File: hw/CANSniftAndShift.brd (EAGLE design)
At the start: 160 x 100 mm, 41 parts, among them CON1 FCI-10033526-N3212LF, CON4 FCI-10033526-N3212LF, IC3 TJA1050, IC4 TJA1050, IC7 FT232RL, Q1 16MHz

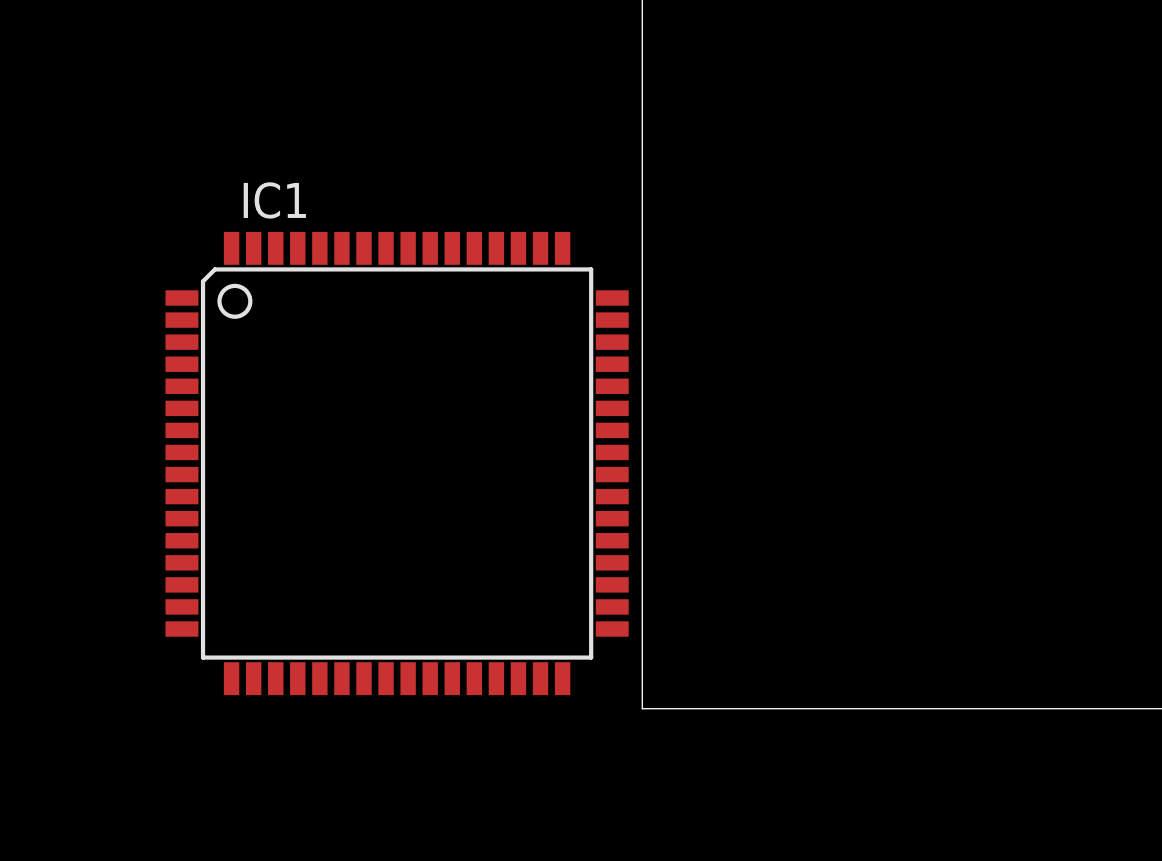
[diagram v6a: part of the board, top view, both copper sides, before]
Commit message: updated lbr AT32 package (wrong footprint used), added Dio driver, modified Port driver
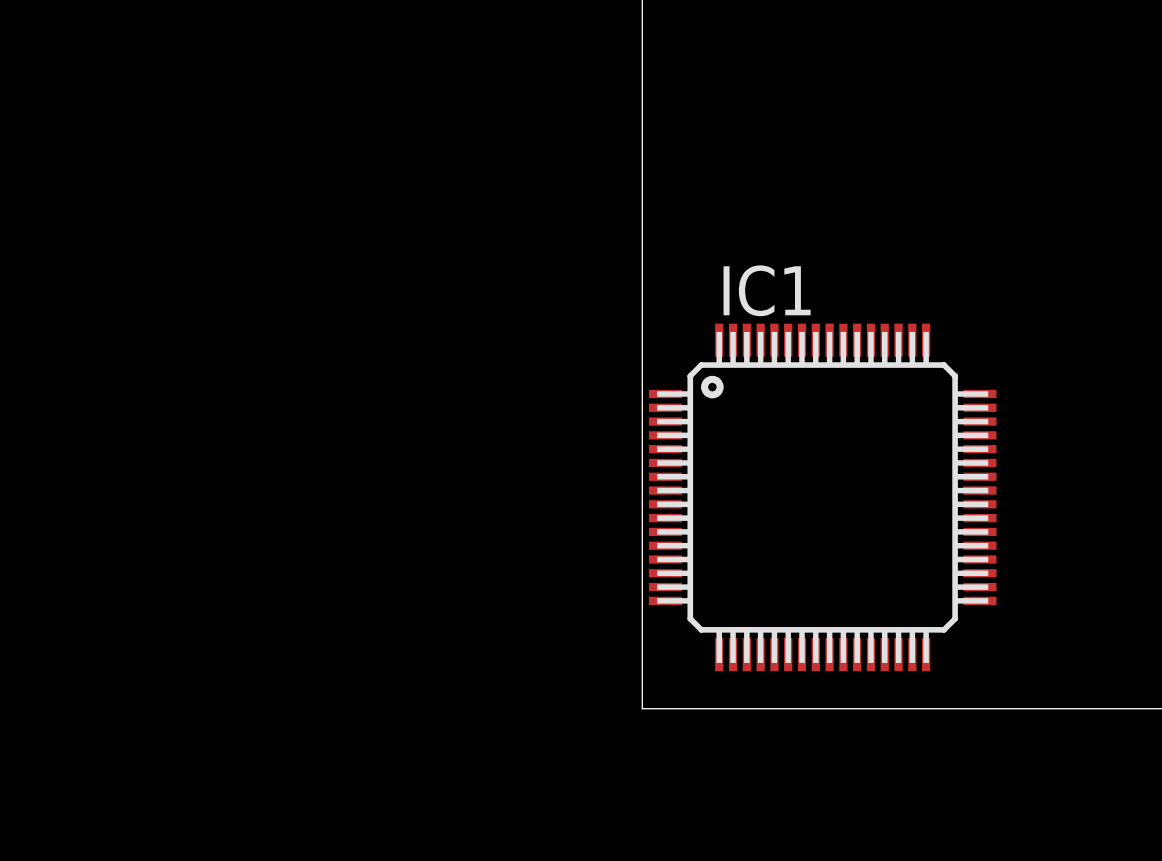
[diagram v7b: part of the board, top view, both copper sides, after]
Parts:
- IC1: device AT32UC3C264C:TQFP64 -> AT32UC3C264C:TQFP64-0.5MM
- moved IC1 15.3 mm to (6.35, 7.62)
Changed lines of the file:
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@@
 </autorouter>
 <elements>
-<element name="IC1" library="AT32UC3C264C" package="TQFP64" value="" x="-8.89" y="8.89"/>
+<element name="IC1" library="AT32UC3C264C" package="TQFP64-0.5MM" value="" x="6.35" y="7.62"/>
 <element name="Q1" library="crystal-abracon-abm3-smd" package="CRYSTAL-ABRACON-ABM7-SMD" value="16MHz" x="-13.97" y="-68.58"/>
 <element name="CON4" library="SchlegelAr_Master" package="FCI-10033526-N3212LF" value="FCI-10033526-N3212LF" x="-11.43" y="-82.55"/>
@@
 <wire x1="-76.73" y1="-306.07" x2="-45.3" y2="-250.19" width="0" layer="19" extent="1-1"/>
 <wire x1="-77.05" y1="-320.04" x2="-76.73" y2="-306.07" width="0" layer="19" extent="1-1"/>
-<wire x1="-14.89" y1="1.09" x2="-15.88" y2="-81.75" width="0" layer="19" extent="1-1"/>
-<wire x1="-7.69" y1="1.09" x2="-14.89" y2="1.09" width="0" layer="19" extent="1-1"/>
-<wire x1="-4.49" y1="1.09" x2="-7.69" y2="1.09" width="0" layer="19" extent="1-1"/>
-<wire x1="-1.09" y1="5.29" x2="-4.49" y2="1.09" width="0" layer="19" extent="1-1"/>
-<wire x1="-16.69" y1="10.89" x2="-14.89" y2="1.09" width="0" layer="19" extent="1-1"/>
-<wire x1="-5.29" y1="16.69" x2="-1.09" y2="5.29" width="0" layer="19" extent="1-1"/>
+<wire x1="2.79" y1="1.96" x2="-15.88" y2="-81.75" width="0" layer="19" extent="1-1"/>
+<wire x1="7.29" y1="1.96" x2="2.79" y2="1.96" width="0" layer="19" extent="1-1"/>
+<wire x1="9.29" y1="1.96" x2="7.29" y2="1.96" width="0" layer="19" extent="1-1"/>
+<wire x1="12.24" y1="5.41" x2="9.29" y2="1.96" width="0" layer="19" extent="1-1"/>
+<wire x1="0.84" y1="8.91" x2="2.79" y2="1.96" width="0" layer="19" extent="1-1"/>
+<wire x1="8.79" y1="13.36" x2="12.24" y2="5.41" width="0" layer="19" extent="1-1"/>
 </signal>
 <signal name="+5V">
@@
 <wire x1="-73.13" y1="-306.07" x2="-39.37" y2="-246.38" width="0" layer="19" extent="1-1"/>
 <wire x1="-76.21" y1="-314.96" x2="-73.13" y2="-306.07" width="0" layer="19" extent="1-1"/>
-<wire x1="-6.89" y1="1.09" x2="-13.03" y2="-81.75" width="0" layer="19" extent="1-1"/>
-<wire x1="-1.09" y1="4.49" x2="-6.89" y2="1.09" width="0" layer="19" extent="1-1"/>
-<wire x1="-4.49" y1="16.69" x2="-1.09" y2="4.49" width="0" layer="19" extent="1-1"/>
-<wire x1="-16.69" y1="11.69" x2="-4.49" y2="16.69" width="0" layer="19" extent="1-1"/>
+<wire x1="7.79" y1="1.96" x2="-13.03" y2="-81.75" width="0" layer="19" extent="1-1"/>
+<wire x1="12.24" y1="4.91" x2="7.79" y2="1.96" width="0" layer="19" extent="1-1"/>
+<wire x1="9.29" y1="13.36" x2="12.24" y2="4.91" width="0" layer="19" extent="1-1"/>
+<wire x1="0.84" y1="9.41" x2="9.29" y2="13.36" width="0" layer="19" extent="1-1"/>
 </signal>
 <signal name="N$2">
 <contactref element="IC1" pad="29"/>
 <contactref element="C11" pad="2"/>
-<wire x1="-5.29" y1="1.09" x2="-14.39" y2="-165.1" width="0" layer="19" extent="1-1"/>
+<wire x1="8.79" y1="1.96" x2="-14.39" y2="-165.1" width="0" layer="19" extent="1-1"/>
 </signal>
 <signal name="N$1">
 <contactref element="IC1" pad="18"/>
 <contactref element="C12" pad="2"/>
-<wire x1="-14.09" y1="1.09" x2="-14.39" y2="-170.18" width="0" layer="19" extent="1-1"/>
+<wire x1="3.29" y1="1.96" x2="-14.39" y2="-170.18" width="0" layer="19" extent="1-1"/>
 </signal>
 <signal name="N$3">
@@
 <contactref element="C13" pad="2"/>
 <wire x1="-11.82" y1="-68.58" x2="-14.39" y2="-154.94" width="0" layer="19" extent="1-1"/>
-<wire x1="-3.69" y1="1.09" x2="-11.82" y2="-68.58" width="0" layer="19" extent="1-1"/>
+<wire x1="9.79" y1="1.96" x2="-11.82" y2="-68.58" width="0" layer="19" extent="1-1"/>
 </signal>
 <signal name="N$4">
@@
 <contactref element="C14" pad="2"/>
 <wire x1="-16.12" y1="-68.58" x2="-14.39" y2="-160.02" width="0" layer="19" extent="1-1"/>
-<wire x1="-2.89" y1="1.09" x2="-16.12" y2="-68.58" width="0" layer="19" extent="1-1"/>
+<wire x1="10.29" y1="1.96" x2="-16.12" y2="-68.58" width="0" layer="19" extent="1-1"/>
 </signal>
 <signal name="USB_D-">
@@
 <contactref element="IC7" pad="1"/>
 <contactref element="IC1" pad="59"/>
-<wire x1="-10.89" y1="16.69" x2="-14.385" y2="-100.145" width="0" layer="19" extent="1-1"/>
+<wire x1="5.29" y1="13.36" x2="-14.385" y2="-100.145" width="0" layer="19" extent="1-1"/>
 </signal>
 <signal name="FTDI_RXD">
 <contactref element="IC7" pad="5"/>
 <contactref element="IC1" pad="58"/>
-<wire x1="-10.09" y1="16.69" x2="-11.785" y2="-100.145" width="0" layer="19" extent="1-1"/>
+<wire x1="5.79" y1="13.36" x2="-11.785" y2="-100.145" width="0" layer="19" extent="1-1"/>
 </signal>
 <signal name="FTDI_3V3OUT">
@@
 <contactref element="IC1" pad="45"/>
 <contactref element="IC3" pad="4"/>
-<wire x1="-40.005" y1="-216.4334" x2="-1.09" y2="12.49" width="0" layer="19" extent="1-1"/>
+<wire x1="-40.005" y1="-216.4334" x2="12.24" y2="9.91" width="0" layer="19" extent="1-1"/>
 </signal>
 <signal name="CAN0TX">
 <contactref element="IC1" pad="46"/>
 <contactref element="IC3" pad="1"/>
-<wire x1="-43.815" y1="-216.4334" x2="-1.09" y2="13.29" width="0" layer="19" extent="1-1"/>
+<wire x1="-43.815" y1="-216.4334" x2="12.24" y2="10.41" width="0" layer="19" extent="1-1"/>
 </signal>
 <signal name="USB_DP">
 <contactref element="IC1" pad="25"/>
 <contactref element="CON1" pad="3"/>
-<wire x1="-8.49" y1="1.09" x2="-22.86" y2="-194.78" width="0" layer="19" extent="1-1"/>
+<wire x1="6.79" y1="1.96" x2="-22.86" y2="-194.78" width="0" layer="19" extent="1-1"/>
 </signal>
 <signal name="USB_DM">
 <contactref element="IC1" pad="24"/>
 <contactref element="CON1" pad="2"/>
-<wire x1="-9.29" y1="1.09" x2="-23.66" y2="-194.78" width="0" layer="19" extent="1-1"/>
+<wire x1="6.29" y1="1.96" x2="-23.66" y2="-194.78" width="0" layer="19" extent="1-1"/>
 </signal>
 <signal name="USB_VBUS">
@@
 <contactref element="JP1" pad="1"/>
 <wire x1="-24.46" y1="-194.78" x2="-33.02" y2="-201.93" width="0" layer="19" extent="1-1"/>
-<wire x1="-10.09" y1="1.09" x2="-24.46" y2="-194.78" width="0" layer="19" extent="1-1"/>
+<wire x1="5.79" y1="1.96" x2="-24.46" y2="-194.78" width="0" layer="19" extent="1-1"/>
 </signal>
 <signal name="!RESET">
@@
 <wire x1="-38.6588" y1="-200.3806" x2="-45.1612" y2="-200.3806" width="0" layer="19" extent="1-1"/>
 <wire x1="-17.78" y1="-186.69" x2="-38.6588" y2="-200.3806" width="0" layer="19" extent="1-1"/>
-<wire x1="-14.89" y1="16.69" x2="-17.78" y2="-186.69" width="0" layer="19" extent="1-1"/>
+<wire x1="2.79" y1="13.36" x2="-17.78" y2="-186.69" width="0" layer="19" extent="1-1"/>
 </signal>
 <signal name="JTAG_TCK">
 <contactref element="SV1" pad="1"/>
 <contactref element="IC1" pad="1"/>
-<wire x1="-16.69" y1="14.89" x2="-22.86" y2="-189.23" width="0" layer="19" extent="1-1"/>
+<wire x1="0.84" y1="11.41" x2="-22.86" y2="-189.23" width="0" layer="19" extent="1-1"/>
 </signal>
 <signal name="JTAG_TDO">
 <contactref element="SV1" pad="3"/>
 <contactref element="IC1" pad="3"/>
-<wire x1="-16.69" y1="13.29" x2="-20.32" y2="-189.23" width="0" layer="19" extent="1-1"/>
+<wire x1="0.84" y1="10.41" x2="-20.32" y2="-189.23" width="0" layer="19" extent="1-1"/>
 </signal>
 <signal name="JTAG_TMS">
 <contactref element="SV1" pad="5"/>
 <contactref element="IC1" pad="4"/>
-<wire x1="-16.69" y1="12.49" x2="-17.78" y2="-189.23" width="0" layer="19" extent="1-1"/>
+<wire x1="0.84" y1="9.91" x2="-17.78" y2="-189.23" width="0" layer="19" extent="1-1"/>
 </signal>
 <signal name="JTAG_TDI">
 <contactref element="SV1" pad="9"/>
 <contactref element="IC1" pad="2"/>
-<wire x1="-16.69" y1="14.09" x2="-12.7" y2="-189.23" width="0" layer="19" extent="1-1"/>
+<wire x1="0.84" y1="10.91" x2="-12.7" y2="-189.23" width="0" layer="19" extent="1-1"/>
 </signal>
 <signal name="N$12">
@@
 <contactref element="IC1" pad="39"/>
 <contactref element="IC4" pad="4"/>
-<wire x1="-40.005" y1="-225.3234" x2="-1.09" y2="7.69" width="0" layer="19" extent="1-1"/>
+<wire x1="-40.005" y1="-225.3234" x2="12.24" y2="6.91" width="0" layer="19" extent="1-1"/>
 </signal>
 <signal name="CAN1TX">
 <contactref element="IC1" pad="40"/>
 <contactref element="IC4" pad="1"/>
-<wire x1="-1.09" y1="8.49" x2="-43.815" y2="-225.3234" width="0" layer="19" extent="1-1"/>
+<wire x1="12.24" y1="7.41" x2="-43.815" y2="-225.3234" width="0" layer="19" extent="1-1"/>
 </signal>
 <signal name="SPI0_MOSI">
@@
 <contactref element="C18" pad="2"/>
 <wire x1="-71.11" y1="-314.96" x2="-75.35" y2="-320.04" width="0" layer="19" extent="1-1"/>
-<wire x1="-6.09" y1="1.09" x2="-71.11" y2="-314.96" width="0" layer="19" extent="1-1"/>
+<wire x1="8.29" y1="1.96" x2="-71.11" y2="-314.96" width="0" layer="19" extent="1-1"/>
 </signal>
 </signals>

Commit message: update
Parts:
- moved SV1 239.3 mm to (20.3, 48.3), turned to 270 degrees
- moved C14 237.6 mm to (49.5, 68.6)
- moved C13 223.0 mm to (49.5, 58.4)
- moved Q1 146.6 mm to (49.5, 63.5), turned to 270 degrees
- moved IC1 61.7 mm to (39.4, 59.7), turned to 90 degrees
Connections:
- removed net N$1: C12.2, IC1.18
- net +5V: now also C12.2, IC1.18
